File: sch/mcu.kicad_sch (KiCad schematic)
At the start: 20 parts, among them U201 STM32F446ZCTx, Y201 Crystal_GND24

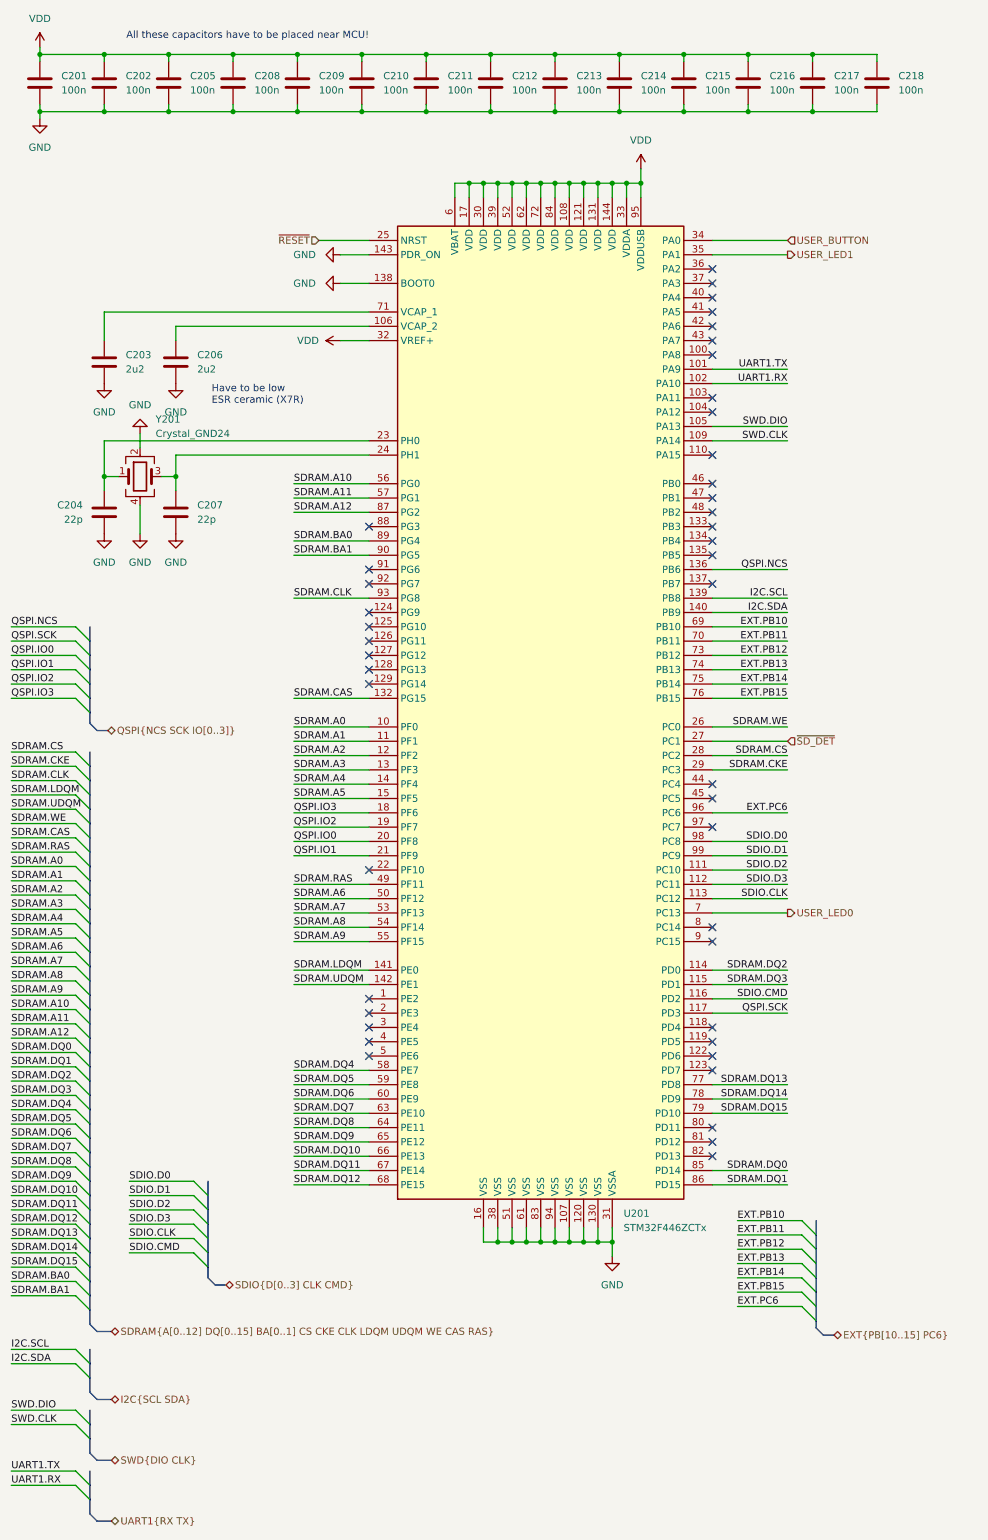
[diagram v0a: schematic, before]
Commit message: Added more expansion capability.
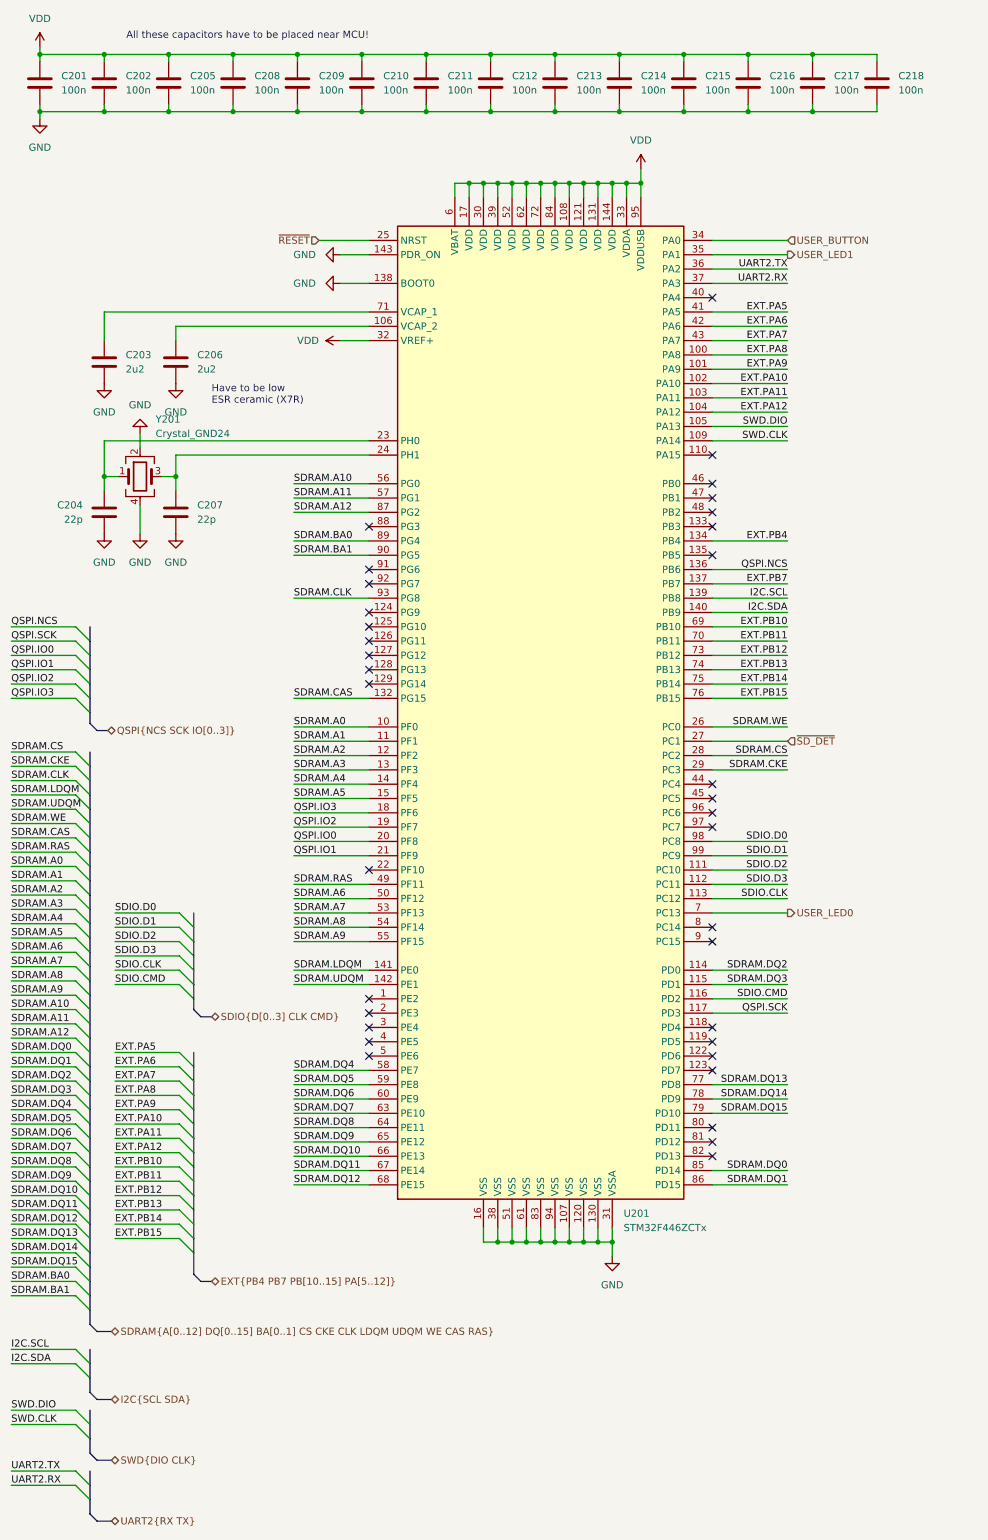
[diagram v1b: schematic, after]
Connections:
- net EXT.PA8: now reaches U201.100 (PA8)
- net EXT.PA11: now reaches U201.103 (PA11)
- net EXT.PA12: now reaches U201.104 (PA12)
- net EXT.PB4: now reaches U201.134 (PB4)
- net EXT.PB7: now reaches U201.137 (PB7)
- net UART2.TX: now reaches U201.36 (PA2)
- net UART2.RX: now reaches U201.37 (PA3)
- net EXT.PA5: now reaches U201.41 (PA5)
- net EXT.PA6: now reaches U201.42 (PA6)
- net EXT.PA7: now reaches U201.43 (PA7)
- net EXT.PC6: no longer names the net of U201.96 (PC6)
- net UART1.RX renamed EXT.PA10
- net UART1.TX renamed EXT.PA9
- no-connect marks 44 -> 35
